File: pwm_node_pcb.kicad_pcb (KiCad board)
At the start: 4 copper layers, 41.5 x 35.3 mm, 38 parts, among them J1 CAN1, J2 TC2050-IDC-NL, J3 Battery, U1 LMR51430, U2 TJA1051T/3, U3 LD1117S33CTR, U4 STM32L432KCU, U5 TXB0104QPWRQ1, Y1 ECS-2520MV-080-BN

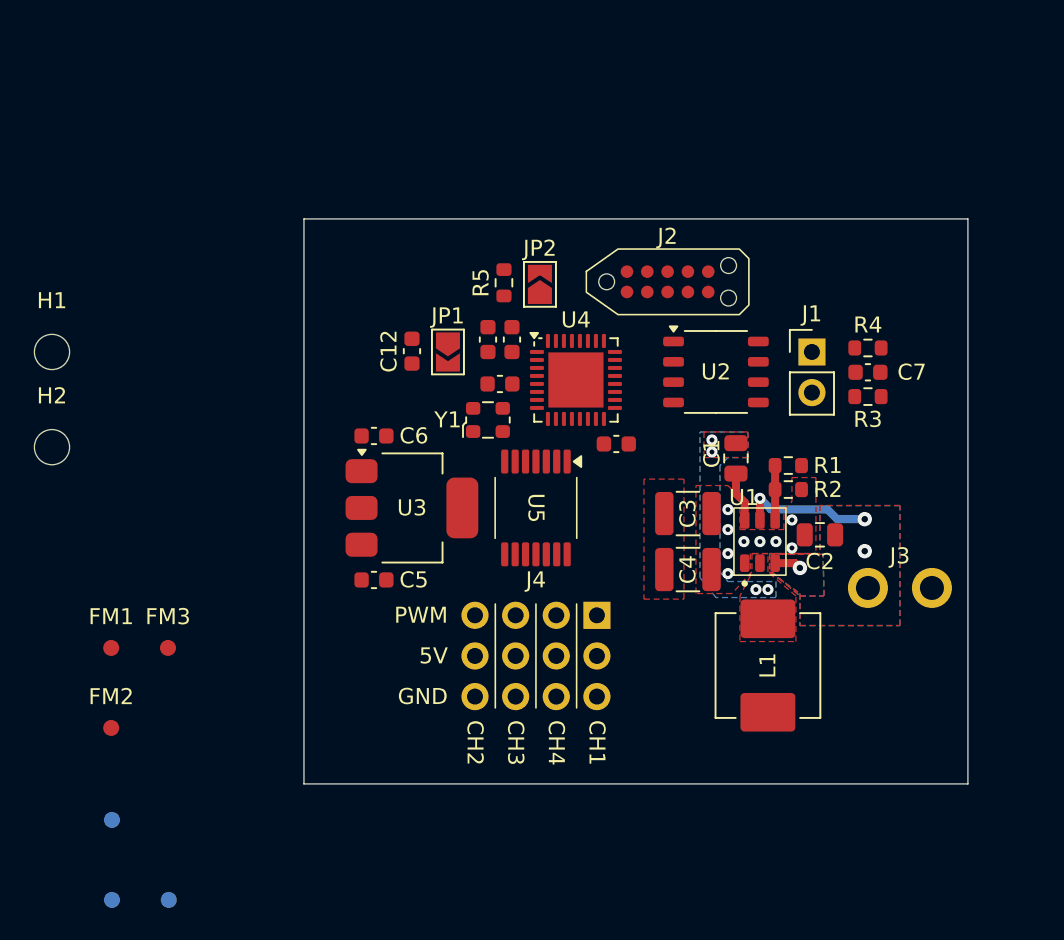
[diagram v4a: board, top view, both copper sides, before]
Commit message: Split load supply and rough placement
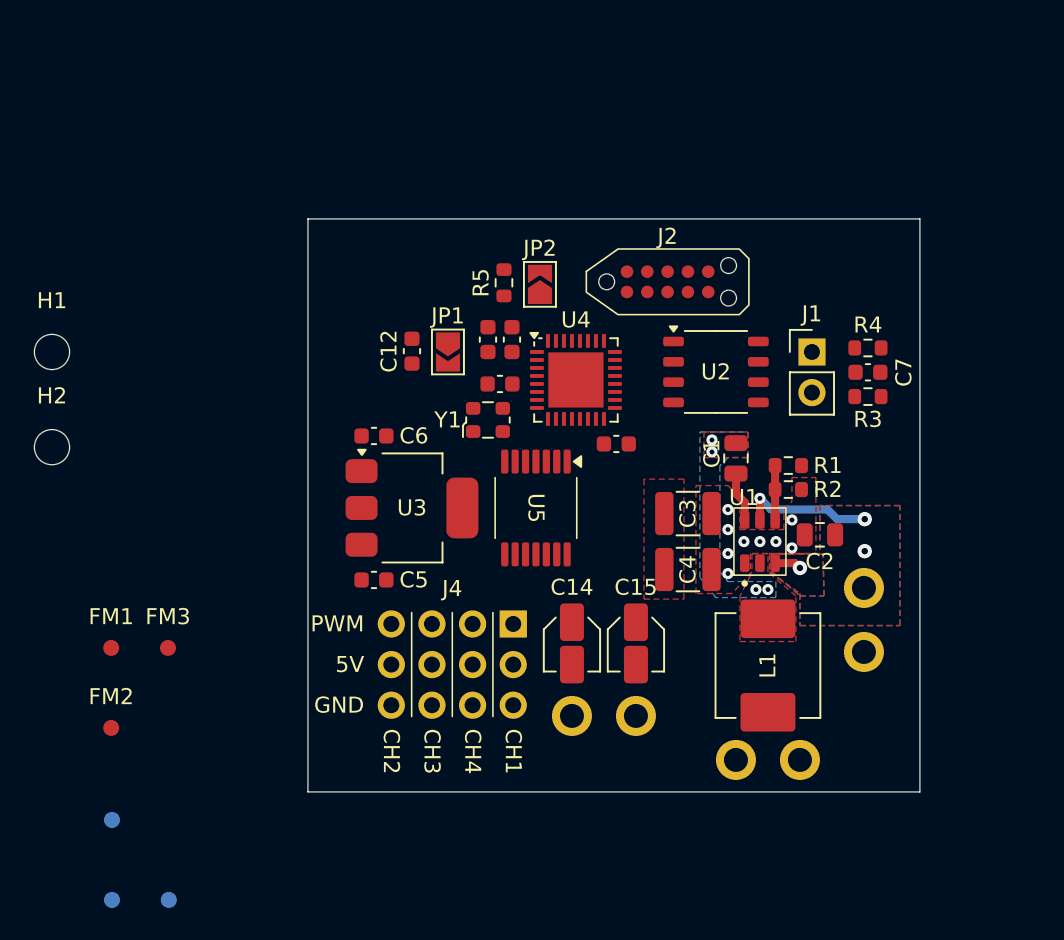
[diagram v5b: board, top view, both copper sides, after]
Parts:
- added C14: 2200u, Capacitor_SMD:C_Elec_3x5.4, F.Cu at (148.2, 121.5)
- added C15: 2200u, Capacitor_SMD:C_Elec_3x5.4, F.Cu at (152.2, 121.5)
- added J5: Load Source, pwm_node_connectors:battery, B.Cu at (150.2, 126.0)
- added J6: 5V Breakout, pwm_node_connectors:battery, B.Cu at (160.5, 128.8)
- J3: moved to B.Cu
- moved J4 5.26 mm to (140.8, 122.8)
- moved J3 3.01 mm to (166.5, 120.0), turned to -90 degrees
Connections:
- J4 pad 11: +5V -> +V_LOAD
- J4 pad 2: +5V -> +V_LOAD
- J4 pad 5: +5V -> +V_LOAD
- J4 pad 8: +5V -> +V_LOAD
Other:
- board size 41.5 x 35.3 mm -> 38.2 x 35.8 mm

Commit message: Pass ERC and DRC, initial v0.1.0-alpha
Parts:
- moved H2 58.9 mm to (173.8, 98.8)
- moved FM6 55.1 mm to (173.8, 127.8)
- moved FM3 51.1 mm to (173.8, 127.8)
- moved FM4 42.2 mm to (139.8, 98.8)
- moved FM1 30.7 mm to (139.8, 98.8)
- moved H1 26.0 mm to (139.8, 113.2)
- moved FM5 20.8 mm to (139.8, 127.8)
- moved FM2 20.3 mm to (139.8, 127.8)
- moved C3 19.5 mm to (173.6, 120.8), turned to 0 degrees
- moved C1 18.8 mm to (170.6, 124.3), turned to -90 degrees
- moved C4 18.1 mm to (173.6, 117.3), turned to 0 degrees
- moved U3 16.4 mm to (154.7, 114.0)
- moved R1 14.6 mm to (167.3, 123.8), turned to 180 degrees
- moved C6 14.1 mm to (149.4, 112.5), turned to 90 degrees
- moved L1 14.0 mm to (168.6, 111.3), turned to 90 degrees
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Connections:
- JP2 pad 1: /BOOT0 -> +3V3
- JP2 pad 2: +3V3 -> /BOOT0
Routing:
- net GND: track 0.00 -> 24.9 mm, vias 9 -> 37
- net +3V3: track 0.00 -> 24.4 mm, vias 0 -> 11
- net /NRST: track 0.00 -> 21.1 mm, vias 0 -> 2
- net +5V: track 0.00 -> 15.9 mm, vias 0 -> 3
- net /SWO: track 0.00 -> 12.3 mm
- net /CAN1-: track 0.00 -> 7.07 mm
- net /CAN1+: track 0.00 -> 7.04 mm
- net /SWCLK: track 0.00 -> 6.76 mm
- net /BOOT0: track 0.00 -> 5.27 mm
- net /PWM2_{5V}: track 0.00 -> 5.27 mm
- net /PWM1_{5V}: track 0.00 -> 5.20 mm
- net /SWDIO: track 0.00 -> 4.95 mm, vias 0 -> 2
- net /PWM3_{5V}: track 0.00 -> 4.48 mm
- net /PWM4_{5V}: track 0.00 -> 4.42 mm
- net /TIM1_CH2: track 0.00 -> 4.15 mm
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- added copper zone on B.Cu, net +3V3
- added copper zone on F.Cu, net +3V3
- added copper zone on B.Cu, net +5V
- added copper zone on B.Cu, net +V_LOAD
- added copper zone on F.Cu, net +V_LOAD
- added copper zone on In1.Cu, net GND
- added copper zone on In2.Cu, net GND
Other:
- board size 38.2 x 35.8 mm -> 40 x 35 mm
- board text added: "CANH"
- board text added: "CANL"
- board text added: "V+"
- board text added: "V_{L}+"
